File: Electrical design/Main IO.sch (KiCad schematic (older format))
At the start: 98 parts, among them P201 10 A, P202 mA, P203 V R, P204 COMMON, Q201 Q_NMOS_GSD, U201 CT138, U202 MCP6002, U203 MCP6N11, U204 74LVC1G66 GNDA, U205 CT138, U206 74LVC1G66 GNDA, U207 TSV634, U208 74LVC1G66 GNDA, U209 74LVC1G66 GNDA, U210 74LVC1G66 GNDA, U211 74LVC1G66 GNDA, U212 74LVC1G66 GNDA, U213 74LVC1G66 GNDA, U214 74LVC1G66 GNDA, U215 74LVC1G66 GNDA, U216 74LVC1G66 GNDA, U217 74LVC1G66 GNDA, U218 74LVC1G66 GNDA

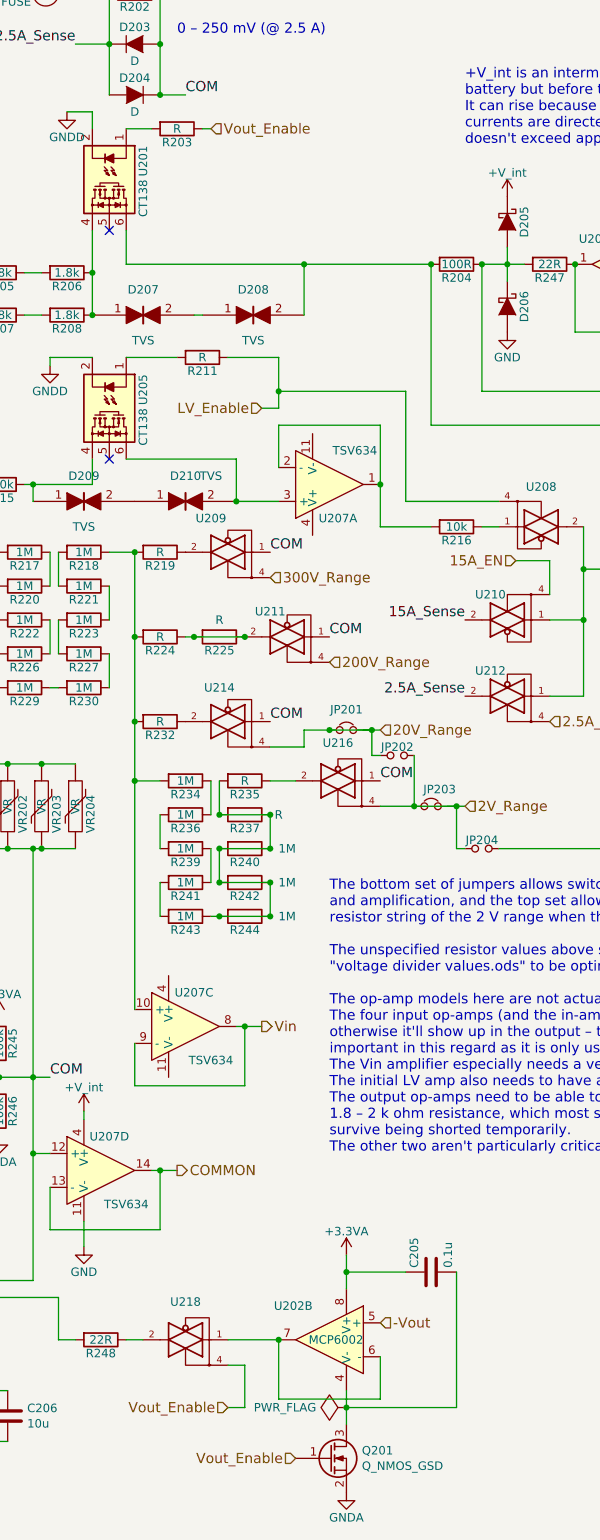
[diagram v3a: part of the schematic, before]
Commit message: Added PCB layout.
Also minor changes to schematic, the most major being changes
to which MCU pins control what to make the PCB layout easier.
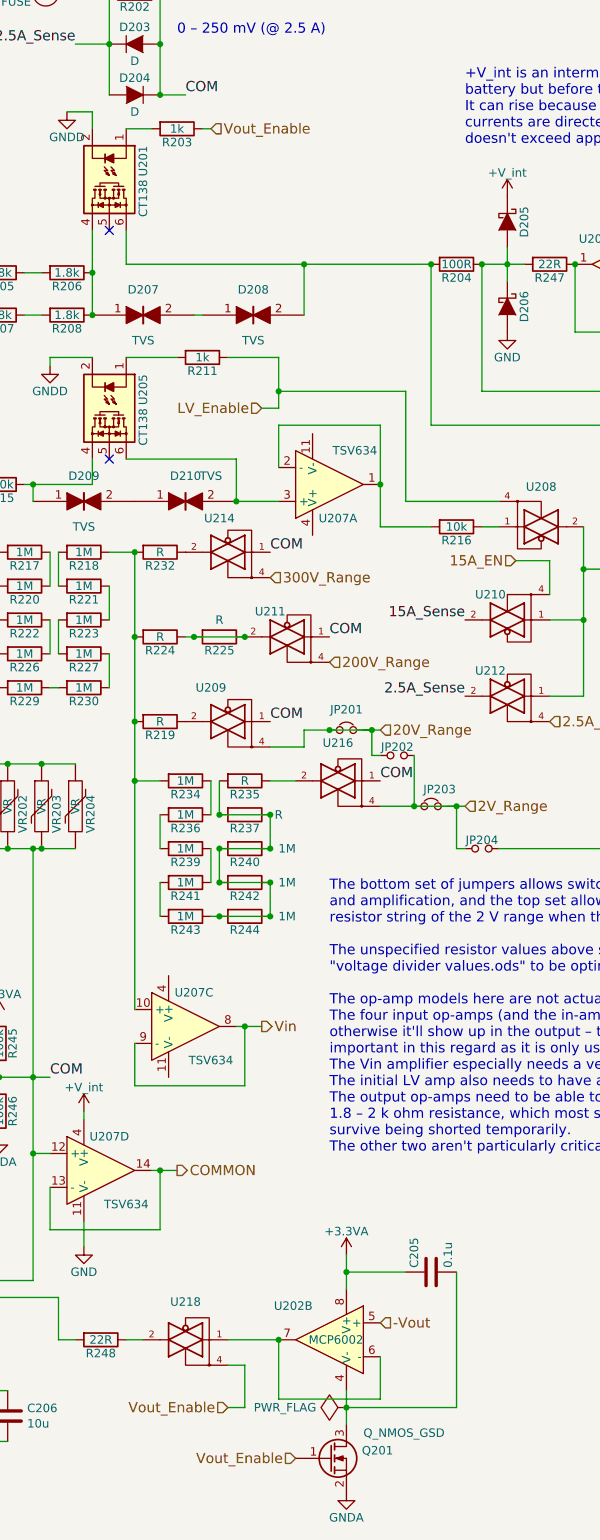
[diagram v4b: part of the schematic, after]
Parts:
- R203, R211: value R -> 1k
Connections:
- net 20V_Range: now also U209.4; no longer U214.4
- net 300V_Range: now also U214.4; no longer U209.4
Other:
- moved on the sheet: R219, R232, U209, U214
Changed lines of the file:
@@
 Sheet 2 5
 Title "Main I/O"
-Date "2016-06-22"
-Rev "0.5"
+Date "2016-07-02"
+Rev "0.6"
 Comp ""
-Comment1 ""
+Comment1 "Licensed under the GNU GPL v3"
 Comment2 ""
 Comment3 ""
@@
 L R R232
 U 1 1 57371F5D
+P 2100 4950
+F 0 "R232" V 2180 4950 50  0000 C CNN
+F 1 "R" V 2100 4950 50  0000 C CNN
+F 2 "my footprints:SMDuniversal_0603to1210_HandSoldering" V 2030 4950 50  0001 C CNN
+F 3 "" H 2100 4950 50  0000 C CNN
+	1    2100 4950
+	0    1    1    0
+$EndComp
+$Comp
+L R R219
+U 1 1 57371F70
 P 2100 5950
-F 0 "R232" V 2180 5950 50  0000 C CNN
+F 0 "R219" V 2180 5950 50  0000 C CNN
 F 1 "R" V 2100 5950 50  0000 C CNN
 F 2 "my footprints:SMDuniversal_0603to1210_HandSoldering" V 2030 5950 50  0001 C CNN
 F 3 "" H 2100 5950 50  0000 C CNN
 	1    2100 5950
-	0    1    1    0
-$EndComp
-$Comp
-L R R219
-U 1 1 57371F70
-P 2100 4950
-F 0 "R219" V 2180 4950 50  0000 C CNN
-F 1 "R" V 2100 4950 50  0000 C CNN
-F 2 "my footprints:SMDuniversal_0603to1210_HandSoldering" V 2030 4950 50  0001 C CNN
-F 3 "" H 2100 4950 50  0000 C CNN
-	1    2100 4950
 	0    1    1    0
 $EndComp
@@
 Text Label 3400 6300 0    60   ~ 0
 COM
-Text Label 2750 5950 0    60   ~ 0
+Text Label 2750 4950 0    60   ~ 0
 COM
 Text Label 3100 5450 0    60   ~ 0
 COM
-Text Label 2750 4950 0    60   ~ 0
+Text Label 2750 5950 0    60   ~ 0
 COM
 Text HLabel 3400 9500 2    60   Input ~ 0
 -Vout
 $Comp
-L GND #PWR032
+L GND #PWR031
 U 1 1 573721DD
 P 4150 3650
-F 0 "#PWR032" H 4150 3400 50  0001 C CNN
+F 0 "#PWR031" H 4150 3400 50  0001 C CNN
 F 1 "GND" H 4150 3500 50  0000 C CNN
 F 2 "" H 4150 3650 50  0000 C CNN
@@
 COM
 $Comp
-L +V_int #PWR033
+L +V_int #PWR032
 U 1 1 5737B363
 P 4150 2850
-F 0 "#PWR033" H 4150 2700 50  0001 C CNN
+F 0 "#PWR032" H 4150 2700 50  0001 C CNN
 F 1 "+V_int" H 4150 2990 50  0000 C CNN
 F 2 "" H 4150 2850 50  0000 C CNN
@@
 $EndComp
 $Comp
-L +V_int #PWR034
+L +V_int #PWR033
 U 1 1 5737B88F
 P 950 7700
-F 0 "#PWR034" H 950 7550 50  0001 C CNN
+F 0 "#PWR033" H 950 7550 50  0001 C CNN
 F 1 "+V_int" H 850 7850 50  0000 C CNN
 F 2 "" H 950 7700 50  0000 C CNN
@@
 +V_int is an intermediate voltage, after the\nbattery but before the voltage regulator.\nIt can rise because any significant clamping\ncurrents are directed to it. It is clamped so it\ndoesn't exceed approximately 4.7 V.
 $Comp
-L VCC #PWR035
+L VCC #PWR034
 U 1 1 5737DBBA
 P 5400 3600
-F 0 "#PWR035" H 5400 3450 50  0001 C CNN
+F 0 "#PWR034" H 5400 3450 50  0001 C CNN
 F 1 "VCC" H 5400 3750 50  0000 C CNN
 F 2 "" H 5400 3600 50  0000 C CNN
@@
 P 2350 3800
 F 0 "R211" V 2430 3800 50  0000 C CNN
-F 1 "R" V 2350 3800 50  0000 C CNN
+F 1 "1k" V 2350 3800 50  0000 C CNN
 F 2 "my footprints:SMDuniversal_0603to1210_HandSoldering" V 2280 3800 50  0001 C CNN
 F 3 "" H 2350 3800 50  0000 C CNN
@@
 P 2200 2450
 F 0 "R203" V 2280 2450 50  0000 C CNN
-F 1 "R" V 2200 2450 50  0000 C CNN
+F 1 "1k" V 2200 2450 50  0000 C CNN
 F 2 "my footprints:SMDuniversal_0603to1210_HandSoldering" V 2130 2450 50  0001 C CNN
 F 3 "" H 2200 2450 50  0000 C CNN
@@
 	5500 4000 5400 4000
 $Comp
-L GNDA #PWR036
+L GNDA #PWR035
 U 1 1 573A8247
 P 1150 8400
-F 0 "#PWR036" H 1150 8150 50  0001 C CNN
+F 0 "#PWR035" H 1150 8150 50  0001 C CNN
 F 1 "GNDA" H 1150 8250 50  0000 C CNN
 F 2 "" H 1150 8400 50  0000 C CNN
@@
 $EndComp
 $Comp
-L +3.3VA #PWR037
+L +3.3VA #PWR036
 U 1 1 573A938C
 P 1150 7700
-F 0 "#PWR037" H 1150 7550 50  0001 C CNN
+F 0 "#PWR036" H 1150 7550 50  0001 C CNN
 F 1 "+3.3VA" H 1150 7840 50  0000 C CNN
 F 2 "" H 1150 7700 50  0000 C CNN
@@
 $EndComp
 $Comp
-L GND #PWR038
+L GND #PWR037
 U 1 1 573AA44A
 P 950 8400
-F 0 "#PWR038" H 950 8150 50  0001 C CNN
+F 0 "#PWR037" H 950 8150 50  0001 C CNN
 F 1 "GND" H 950 8250 50  0000 C CNN
 F 2 "" H 950 8400 50  0000 C CNN
@@
 	4000 4800 4100 4800
 $Comp
-L GNDD #PWR039
+L GNDD #PWR038
 U 1 1 573ABBA3
 P 1450 3850
-F 0 "#PWR039" H 1450 3600 50  0001 C CNN
+F 0 "#PWR038" H 1450 3600 50  0001 C CNN
 F 1 "GNDD" H 1450 3700 50  0000 C CNN
 F 2 "" H 1450 3850 50  0000 C CNN
@@
 $EndComp
 $Comp
-L GNDD #PWR040
+L GNDD #PWR039
 U 1 1 573ABD29
 P 1550 2350
-F 0 "#PWR040" H 1550 2100 50  0001 C CNN
+F 0 "#PWR039" H 1550 2100 50  0001 C CNN
 F 1 "GNDD" H 1550 2200 50  0000 C CNN
 F 2 "" H 1550 2350 50  0000 C CNN
@@
 $EndComp
 $Comp
-L +3.3VA #PWR041
+L +3.3VA #PWR040
 U 1 1 573AE254
 P 5700 3600
-F 0 "#PWR041" H 5700 3450 50  0001 C CNN
+F 0 "#PWR040" H 5700 3450 50  0001 C CNN
 F 1 "+3.3VA" H 5700 3740 50  0000 C CNN
 F 2 "" H 5700 3600 50  0000 C CNN
@@
 $EndComp
 $Comp
-L GNDA #PWR042
+L GNDA #PWR041
 U 1 1 573AE493
 P 5700 4400
-F 0 "#PWR042" H 5700 4150 50  0001 C CNN
+F 0 "#PWR041" H 5700 4150 50  0001 C CNN
 F 1 "GNDA" H 5700 4250 50  0000 C CNN
 F 2 "" H 5700 4400 50  0000 C CNN
@@
 $EndComp
 $Comp
-L GNDA #PWR043
+L GNDA #PWR042
 U 1 1 573AE90F
 P 6200 3600
-F 0 "#PWR043" H 6200 3350 50  0001 C CNN
+F 0 "#PWR042" H 6200 3350 50  0001 C CNN
 F 1 "GNDA" H 6200 3450 50  0000 C CNN
 F 2 "" H 6200 3600 50  0000 C CNN
@@
 	5800 4400 5800 4700
 $Comp
-L +V_int #PWR044
+L +V_int #PWR043
 U 1 1 573B1087
 P 1650 8250
-F 0 "#PWR044" H 1650 8100 50  0001 C CNN
+F 0 "#PWR043" H 1650 8100 50  0001 C CNN
 F 1 "+V_int" H 1650 8390 50  0000 C CNN
 F 2 "" H 1650 8250 50  0000 C CNN
@@
 $EndComp
 $Comp
-L GND #PWR045
+L GND #PWR044
 U 1 1 573B11AC
 P 1650 9050
-F 0 "#PWR045" H 1650 8800 50  0001 C CNN
+F 0 "#PWR044" H 1650 8800 50  0001 C CNN
 F 1 "GND" H 1650 8900 50  0000 C CNN
 F 2 "" H 1650 9050 50  0000 C CNN
@@
 $EndComp
 $Comp
-L GND #PWR046
+L GND #PWR045
 U 1 1 574320CF
 P 1000 10300
-F 0 "#PWR046" H 1000 10050 50  0001 C CNN
+F 0 "#PWR045" H 1000 10050 50  0001 C CNN
 F 1 "GND" H 1000 10150 50  0000 C CNN
 F 2 "" H 1000 10300 50  0000 C CNN
@@
 Connection ~ 4550 3250
 $Comp
-L GNDA #PWR047
+L GNDA #PWR046
 U 1 1 5758E3FF
 P 3200 10500
-F 0 "#PWR047" H 3200 10250 50  0001 C CNN
+F 0 "#PWR046" H 3200 10250 50  0001 C CNN
 F 1 "GNDA" H 3200 10350 50  0000 C CNN
 F 2 "" H 3200 10500 50  0000 C CNN
@@
 	3200 9900 3200 10100
 $Comp
-L +3.3VA #PWR048
+L +3.3VA #PWR047
 U 1 1 5758E968
 P 3200 9100
-F 0 "#PWR048" H 3200 8950 50  0001 C CNN
+F 0 "#PWR047" H 3200 8950 50  0001 C CNN
 F 1 "+3.3VA" H 3200 9240 50  0000 C CNN
 F 2 "" H 3200 9100 50  0000 C CNN
@@
 P 3100 10300
 F 0 "Q201" H 3291 10346 50  0000 L CNN
-F 1 "Q_NMOS_GSD" H 3291 10255 50  0000 L CNN
+F 1 "Q_NMOS_GSD" H 3300 10450 50  0000 L CNN
 F 2 "TO_SOT_Packages_SMD:SOT-23" H 3300 10400 50  0001 C CNN
 F 3 "" H 3100 10300 50  0000 C CNN
@@
 $EndComp
 $Comp
-L +V_int #PWR049
+L +V_int #PWR048
 U 1 1 5763C611
 P 1000 9800
-F 0 "#PWR049" H 1000 9650 50  0001 C CNN
+F 0 "#PWR048" H 1000 9650 50  0001 C CNN
 F 1 "+V_int" H 1000 9940 50  0000 C CNN
 F 2 "" H 1000 9800 50  0000 C CNN
@@
 Connection ~ 3200 10000
 $Comp
-L PWR_FLAG #FLG050
+L PWR_FLAG #FLG049
 U 1 1 5767CED2
 P 3200 10000
-F 0 "#FLG050" H 3200 10095 50  0001 C CNN
+F 0 "#FLG049" H 3200 10095 50  0001 C CNN
 F 1 "PWR_FLAG" V 3200 10178 50  0000 L CNN
 F 2 "" H 3200 10000 50  0000 C CNN
@@
 L 74LVC1G66_GNDA U214
 U 1 1 57681493
-P 2500 5950
-F 0 "U214" H 2550 6150 50  0000 C CNN
-F 1 "74LVC1G66 GNDA" H 2500 6175 50  0001 C CNN
-F 2 "TO_SOT_Packages_SMD:SOT-353" H 2500 5950 50  0001 C CNN
-F 3 "" H 2500 5950 50  0000 C CNN
-	1    2500 5950
+P 2500 4950
+F 0 "U214" H 2550 5150 50  0000 C CNN
+F 1 "74LVC1G66 GNDA" H 2500 5175 50  0001 C CNN
+F 2 "TO_SOT_Packages_SMD:SOT-353" H 2500 4950 50  0001 C CNN
+F 3 "" H 2500 4950 50  0000 C CNN
+	1    2500 4950
 	-1   0    0    -1
 $EndComp
@@
 L 74LVC1G66_GNDA U209
 U 1 1 576816CB
-P 2500 4950
-F 0 "U209" H 2600 5150 50  0000 C CNN
-F 1 "74LVC1G66 GNDA" H 2500 5175 50  0001 C CNN
-F 2 "TO_SOT_Packages_SMD:SOT-353" H 2500 4950 50  0001 C CNN
-F 3 "" H 2500 4950 50  0000 C CNN
-	1    2500 4950
+P 2500 5950
+F 0 "U209" H 2600 6150 50  0000 C CNN
+F 1 "74LVC1G66 GNDA" H 2500 6175 50  0001 C CNN
+F 2 "TO_SOT_Packages_SMD:SOT-353" H 2500 5950 50  0001 C CNN
+F 3 "" H 2500 5950 50  0000 C CNN
+	1    2500 5950
 	-1   0    0    -1
 $EndComp

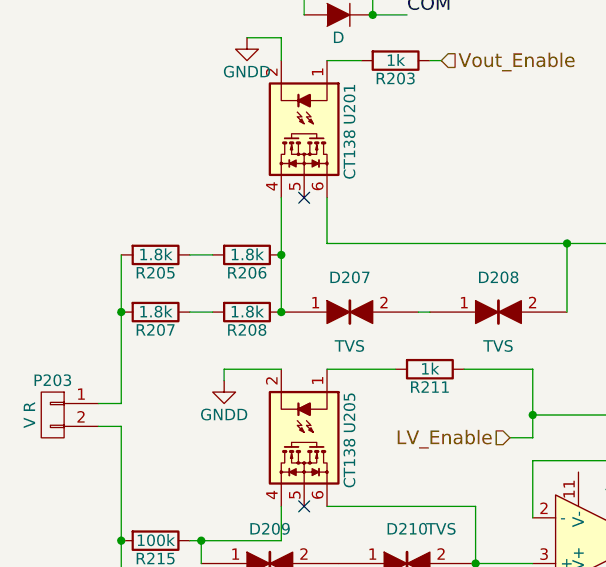
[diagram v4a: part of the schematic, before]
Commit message: Tied ground nets together, fixed clearance issues, added copper pours / zones.
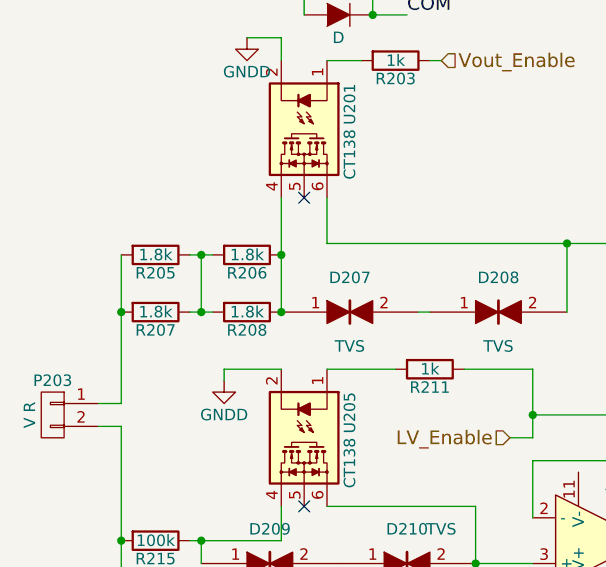
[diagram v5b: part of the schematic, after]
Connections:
- net at R205.1, R206.2: now also R207.1, R208.2
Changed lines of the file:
@@
 Sheet 2 5
 Title "Main I/O"
-Date "2016-07-02"
-Rev "0.6"
+Date "2016-07-04"
+Rev "0.7"
 Comp ""
 Comment1 "Licensed under the GNU GPL v3"
@@
 -Vout
 $Comp
-L GND #PWR031
+L GND #PWR206
 U 1 1 573721DD
 P 4150 3650
-F 0 "#PWR031" H 4150 3400 50  0001 C CNN
+F 0 "#PWR206" H 4150 3400 50  0001 C CNN
 F 1 "GND" H 4150 3500 50  0000 C CNN
 F 2 "" H 4150 3650 50  0000 C CNN
@@
 COM
 $Comp
-L +V_int #PWR032
+L +V_int #PWR202
 U 1 1 5737B363
 P 4150 2850
-F 0 "#PWR032" H 4150 2700 50  0001 C CNN
+F 0 "#PWR202" H 4150 2700 50  0001 C CNN
 F 1 "+V_int" H 4150 2990 50  0000 C CNN
 F 2 "" H 4150 2850 50  0000 C CNN
@@
 $EndComp
 $Comp
-L +V_int #PWR033
+L +V_int #PWR209
 U 1 1 5737B88F
 P 950 7700
-F 0 "#PWR033" H 950 7550 50  0001 C CNN
+F 0 "#PWR209" H 950 7550 50  0001 C CNN
 F 1 "+V_int" H 850 7850 50  0000 C CNN
 F 2 "" H 950 7700 50  0000 C CNN
@@
 +V_int is an intermediate voltage, after the\nbattery but before the voltage regulator.\nIt can rise because any significant clamping\ncurrents are directed to it. It is clamped so it\ndoesn't exceed approximately 4.7 V.
 $Comp
-L VCC #PWR034
+L VCC #PWR203
 U 1 1 5737DBBA
 P 5400 3600
-F 0 "#PWR034" H 5400 3450 50  0001 C CNN
+F 0 "#PWR203" H 5400 3450 50  0001 C CNN
 F 1 "VCC" H 5400 3750 50  0000 C CNN
 F 2 "" H 5400 3600 50  0000 C CNN
@@
 	5500 4000 5400 4000
 $Comp
-L GNDA #PWR035
+L GNDA #PWR213
 U 1 1 573A8247
 P 1150 8400
-F 0 "#PWR035" H 1150 8150 50  0001 C CNN
+F 0 "#PWR213" H 1150 8150 50  0001 C CNN
 F 1 "GNDA" H 1150 8250 50  0000 C CNN
 F 2 "" H 1150 8400 50  0000 C CNN
@@
 $EndComp
 $Comp
-L +3.3VA #PWR036
+L +3.3VA #PWR210
 U 1 1 573A938C
 P 1150 7700
-F 0 "#PWR036" H 1150 7550 50  0001 C CNN
+F 0 "#PWR210" H 1150 7550 50  0001 C CNN
 F 1 "+3.3VA" H 1150 7840 50  0000 C CNN
 F 2 "" H 1150 7700 50  0000 C CNN
@@
 $EndComp
 $Comp
-L GND #PWR037
+L GND #PWR212
 U 1 1 573AA44A
 P 950 8400
-F 0 "#PWR037" H 950 8150 50  0001 C CNN
+F 0 "#PWR212" H 950 8150 50  0001 C CNN
 F 1 "GND" H 950 8250 50  0000 C CNN
 F 2 "" H 950 8400 50  0000 C CNN
@@
 	4000 4800 4100 4800
 $Comp
-L GNDD #PWR038
+L GNDD #PWR207
 U 1 1 573ABBA3
 P 1450 3850
-F 0 "#PWR038" H 1450 3600 50  0001 C CNN
+F 0 "#PWR207" H 1450 3600 50  0001 C CNN
 F 1 "GNDD" H 1450 3700 50  0000 C CNN
 F 2 "" H 1450 3850 50  0000 C CNN
@@
 $EndComp
 $Comp
-L GNDD #PWR039
+L GNDD #PWR201
 U 1 1 573ABD29
 P 1550 2350
-F 0 "#PWR039" H 1550 2100 50  0001 C CNN
+F 0 "#PWR201" H 1550 2100 50  0001 C CNN
 F 1 "GNDD" H 1550 2200 50  0000 C CNN
 F 2 "" H 1550 2350 50  0000 C CNN
@@
 $EndComp
 $Comp
-L +3.3VA #PWR040
+L +3.3VA #PWR204
 U 1 1 573AE254
 P 5700 3600
-F 0 "#PWR040" H 5700 3450 50  0001 C CNN
+F 0 "#PWR204" H 5700 3450 50  0001 C CNN
 F 1 "+3.3VA" H 5700 3740 50  0000 C CNN
 F 2 "" H 5700 3600 50  0000 C CNN
@@
 $EndComp
 $Comp
-L GNDA #PWR041
+L GNDA #PWR208
 U 1 1 573AE493
 P 5700 4400
-F 0 "#PWR041" H 5700 4150 50  0001 C CNN
+F 0 "#PWR208" H 5700 4150 50  0001 C CNN
 F 1 "GNDA" H 5700 4250 50  0000 C CNN
 F 2 "" H 5700 4400 50  0000 C CNN
@@
 $EndComp
 $Comp
-L GNDA #PWR042
+L GNDA #PWR205
 U 1 1 573AE90F
 P 6200 3600
-F 0 "#PWR042" H 6200 3350 50  0001 C CNN
+F 0 "#PWR205" H 6200 3350 50  0001 C CNN
 F 1 "GNDA" H 6200 3450 50  0000 C CNN
 F 2 "" H 6200 3600 50  0000 C CNN
@@
 	5800 4400 5800 4700
 $Comp
-L +V_int #PWR043
+L +V_int #PWR211
 U 1 1 573B1087
 P 1650 8250
-F 0 "#PWR043" H 1650 8100 50  0001 C CNN
+F 0 "#PWR211" H 1650 8100 50  0001 C CNN
 F 1 "+V_int" H 1650 8390 50  0000 C CNN
 F 2 "" H 1650 8250 50  0000 C CNN
@@
 $EndComp
 $Comp
-L GND #PWR044
+L GND #PWR214
 U 1 1 573B11AC
 P 1650 9050
-F 0 "#PWR044" H 1650 8800 50  0001 C CNN
+F 0 "#PWR214" H 1650 8800 50  0001 C CNN
 F 1 "GND" H 1650 8900 50  0000 C CNN
 F 2 "" H 1650 9050 50  0000 C CNN
@@
 $EndComp
 $Comp
-L GND #PWR045
+L GND #PWR217
 U 1 1 574320CF
 P 1000 10300
-F 0 "#PWR045" H 1000 10050 50  0001 C CNN
+F 0 "#PWR217" H 1000 10050 50  0001 C CNN
 F 1 "GND" H 1000 10150 50  0000 C CNN
 F 2 "" H 1000 10300 50  0000 C CNN
@@
 Connection ~ 4550 3250
 $Comp
-L GNDA #PWR046
+L GNDA #PWR218
 U 1 1 5758E3FF
 P 3200 10500
-F 0 "#PWR046" H 3200 10250 50  0001 C CNN
+F 0 "#PWR218" H 3200 10250 50  0001 C CNN
 F 1 "GNDA" H 3200 10350 50  0000 C CNN
 F 2 "" H 3200 10500 50  0000 C CNN
@@
 	3200 9900 3200 10100
 $Comp
-L +3.3VA #PWR047
+L +3.3VA #PWR215
 U 1 1 5758E968
 P 3200 9100
-F 0 "#PWR047" H 3200 8950 50  0001 C CNN
+F 0 "#PWR215" H 3200 8950 50  0001 C CNN
 F 1 "+3.3VA" H 3200 9240 50  0000 C CNN
 F 2 "" H 3200 9100 50  0000 C CNN
@@
 $EndComp
 $Comp
-L +V_int #PWR048
+L +V_int #PWR216
 U 1 1 5763C611
 P 1000 9800
-F 0 "#PWR048" H 1000 9650 50  0001 C CNN
+F 0 "#PWR216" H 1000 9650 50  0001 C CNN
 F 1 "+V_int" H 1000 9940 50  0000 C CNN
 F 2 "" H 1000 9800 50  0000 C CNN
@@
 Connection ~ 3200 10000
 $Comp
-L PWR_FLAG #FLG049
+L PWR_FLAG #FLG201
 U 1 1 5767CED2
 P 3200 10000
-F 0 "#FLG049" H 3200 10095 50  0001 C CNN
+F 0 "#FLG201" H 3200 10095 50  0001 C CNN
 F 1 "PWR_FLAG" V 3200 10178 50  0000 L CNN
 F 2 "" H 3200 10000 50  0000 C CNN
@@
 	-1   0    0    -1
 $EndComp
+Wire Wire Line
+	1350 3300 1350 3550
+Connection ~ 1350 3550
+Connection ~ 1350 3300
 $EndSCHEMATC

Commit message: Add documentation. Fix some issues found while writing it.
The issues fixed:
Change R245-246 to 1M.
Remove D211-212 and add D213-214.
Power the analog switches from +V_int.
Reconfigure range combination jumpers.
Remove "GND" net.
Correct values of C103-105, and add R106-108 (correcting values of R101-103).
Change +V_int around to be based of +3.3VA instead of +BATT, and clamp to 3.5 V.
Along with above, remove GND rail, mostly replacing with GNDA.
Update PCB for changes.
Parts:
- removed D211, D212: D_Schottky, my footprints:SC-90A, symbol D_Schottky
- added D213, D214: D_Schottky, my footprints:SC-90A, symbol D_Schottky
- JP201, JP203: value Jumper_NC_Small -> Jumper_NO_Small; symbol Jumper_NC_Small -> Jumper_NO_Small
- JP202, JP204: value Jumper_NO_Small -> Jumper_NC_Small; symbol Jumper_NO_Small -> Jumper_NC_Small
- R245, R246: value 100k -> 1M
- R247, R248: value 22R -> 68R
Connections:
- net GND is gone; now on net GNDA: C202.2, C206.1, D206.2 (A), U207.11 (V-)
- net +3.3VA: no longer U204.5 (VCC), U206.5 (VCC), U208.5 (VCC), U209.5 (VCC), U210.5 (VCC), U211.5 (VCC), U212.5 (VCC), U213.5 (VCC), U214.5 (VCC), U215.5 (VCC), U216.5 (VCC), U217.5 (VCC), U218.5 (VCC)
- net +V_int: now also U204.5 (VCC), U206.5 (VCC), U208.5 (VCC), U209.5 (VCC), U210.5 (VCC), U211.5 (VCC), U212.5 (VCC), U213.5 (VCC), U214.5 (VCC), U215.5 (VCC), U216.5 (VCC), U217.5 (VCC), U218.5 (VCC), D213.1 (K)
- net 20V_Range: now also JP202.2, JP203.1, U216.4; no longer JP201.1, U209.4
- net 2V_Range: now also JP204.2, U217.4; no longer JP202.2, JP203.1, U216.4
- net GNDA: now also D214.2 (A)
- net at P204.2 (P2): now also U218.2, D213.2 (A), D214.1 (K); no longer R248.2
- net at U202.6 (-), U202.7: now also R248.1; no longer U218.1
- new net: JP201.1, U209.4
- new net: R248.2, U218.1
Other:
- note added: "The bottom set of jumpers allows switching the 2 V range between attenuation\nand amplification, and the top set allows switching the 20 V range to use the\nresistor string of the 2 V range when the 2 V range is set for amplification.\nCurrently the 2 V range is used for amplification, and the 20 V range uses the long string.\n\nThe unspecified resistor values above should be calculated using the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"
- note removed: "+V_int is an intermediate voltage, after the\nbattery but before the voltage regulator.\nIt can rise because any significant clamping\ncurrents are directed to it. It is clamped so it\ndoesn't exceed approximately 4.7 V."
- note removed: "The bottom set of jumpers allows switching the 2 V range between attenuation\nand amplification, and the top set allows switching the 20 V range to use the\nresistor string of the 2 V range when the 2 V range is set for amplification.\n\nThe unspecified resistor values above should be calculated using the spreadsheet\n"voltage divider values.ods" to be optimised for resolution of the primary ADC.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"
- moved on the sheet: C205, Q201, R248, U202B, U218
